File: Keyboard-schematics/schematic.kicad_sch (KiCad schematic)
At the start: 26 parts, among them J1 USB_C_Receptacle_USB2.0, J2 Conn_01x05, J3 Conn_01x04, U1 STM32F072CBT6, U2 PRTR5V0U2X, U3 XC6206PxxxMR-Regulator_Linear, U5 TXB0101

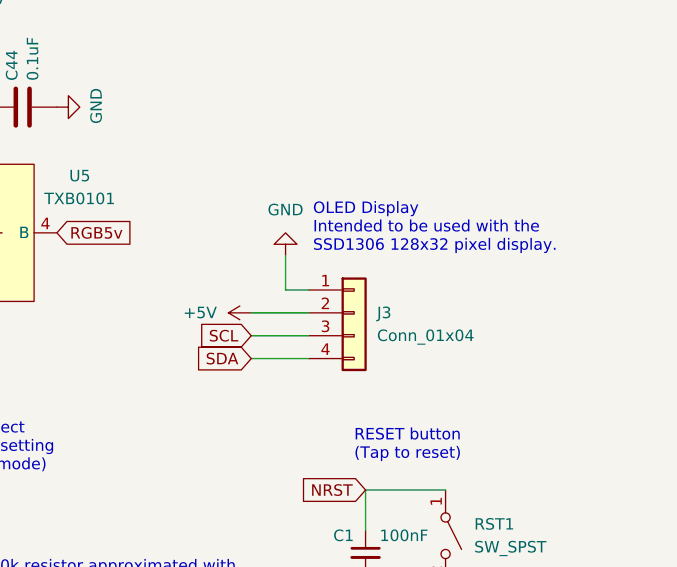
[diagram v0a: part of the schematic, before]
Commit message: Assigned footprints to diodes
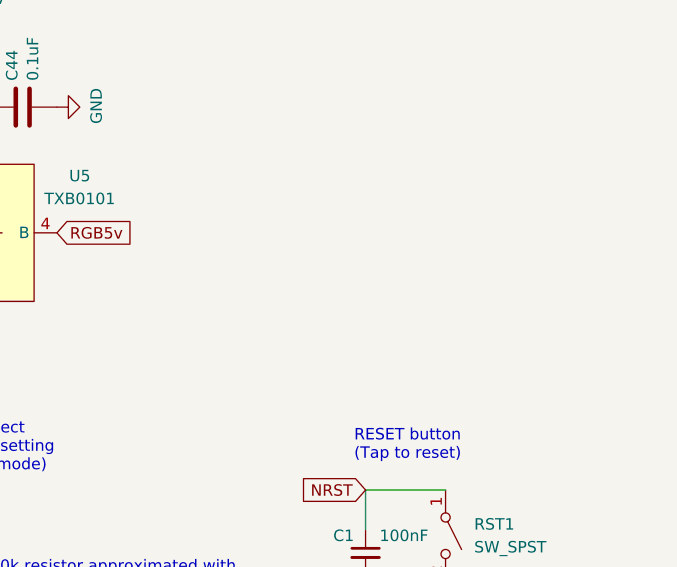
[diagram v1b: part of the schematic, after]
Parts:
- removed J3: Conn_01x04, KiCad-SSD1306-0.91-OLED-4pin-128x32.pretty-master:SSD1306-0.91-OLED-4pin-128x32, symbol Connector_Generic:Conn_01x04
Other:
- note removed: "OLED Display Intended to be used with the SSD1306 128x32 pixel display."

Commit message: Alternative layout wiring
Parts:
- U5: footprint Package_TO_SOT_SMD:SOT-363_SC-70-6_Handsoldering -> Package_TO_SOT_SMD:SOT-363_SC-70-6
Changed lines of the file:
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@@
 			)
 		)
-		(property "Footprint" "Package_TO_SOT_SMD:SOT-363_SC-70-6_Handsoldering"
+		(property "Footprint" "Package_TO_SOT_SMD:SOT-363_SC-70-6"
 			(at 209.55 121.92 0)
 			(effects
